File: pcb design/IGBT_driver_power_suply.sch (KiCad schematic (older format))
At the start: 41 parts, among them Q15 CSD19533Q5A, Q16 CSD19533Q5A, T1 TRANS-3-1CT, U2 LM5030

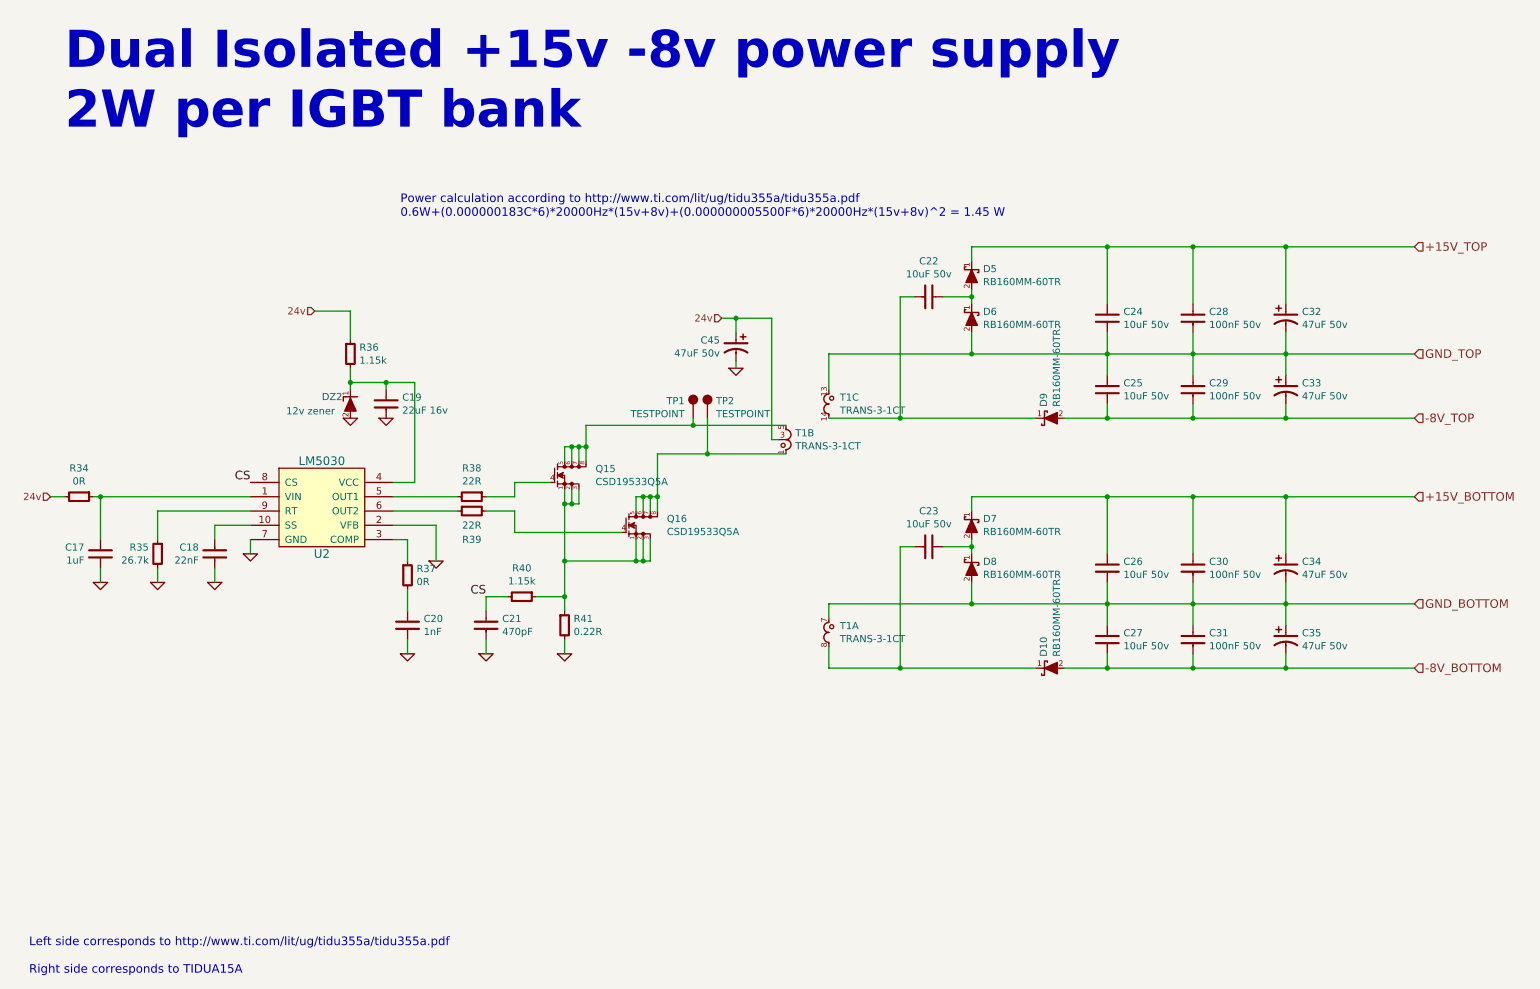
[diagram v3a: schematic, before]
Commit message: Added testpoints
Signed-off-by: Marcos Chaparro <mchaparro@paltatech.com>
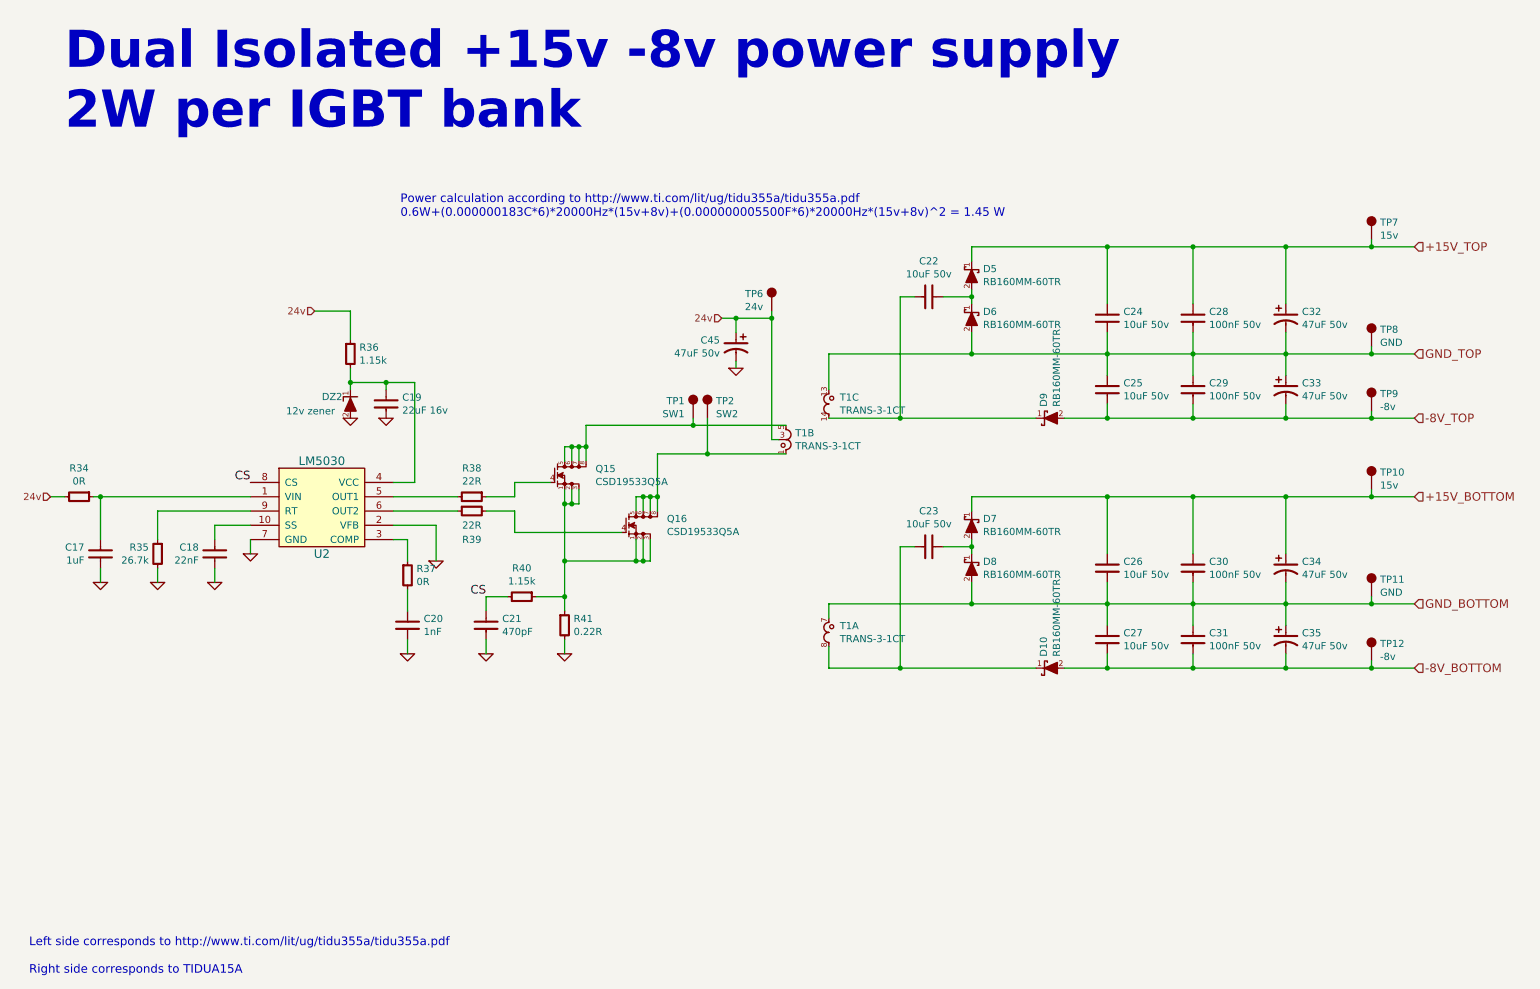
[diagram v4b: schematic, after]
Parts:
- added TP10, TP7: 15v, conn-test:TEST-SMD-SMALL, symbol TESTPOINT
- added TP11, TP8: GND, conn-test:TEST-SMD-SMALL, symbol TESTPOINT
- added TP12, TP9: -8v, conn-test:TEST-SMD-SMALL, symbol TESTPOINT
- added TP6: 24v, conn-test:TEST-SMD-SMALL, symbol TESTPOINT
- TP1: value TESTPOINT -> SW1
- TP2: value TESTPOINT -> SW2
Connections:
- net +15V_BOTTOM: now also TP10.1
- net +15V_TOP: now also TP7.1
- net -8V_BOTTOM: now also TP12.1
- net -8V_TOP: now also TP9.1
- net 24v: now also TP6.1
- net GND_BOTTOM: now also TP11.1
- net GND_TOP: now also TP8.1
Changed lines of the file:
@@
 $EndComp
 $Comp
-L GND #PWR06
+L GND #PWR11
 U 1 1 582356E3
 P 2950 3500
-F 0 "#PWR06" H 2950 3500 30  0001 C CNN
+F 0 "#PWR11" H 2950 3500 30  0001 C CNN
 F 1 "GND" H 2950 3430 30  0001 C CNN
 F 2 "" H 2950 3500 60  0000 C CNN
@@
 $EndComp
 $Comp
-L GND #PWR07
+L GND #PWR12
 U 1 1 58235BA0
 P 3200 3500
-F 0 "#PWR07" H 3200 3500 30  0001 C CNN
+F 0 "#PWR12" H 3200 3500 30  0001 C CNN
 F 1 "GND" H 3200 3430 30  0001 C CNN
 F 2 "" H 3200 3500 60  0000 C CNN
@@
 $EndComp
 $Comp
-L GND #PWR08
+L GND #PWR9
 U 1 1 58235E8A
 P 2000 4650
-F 0 "#PWR08" H 2000 4650 30  0001 C CNN
+F 0 "#PWR9" H 2000 4650 30  0001 C CNN
 F 1 "GND" H 2000 4580 30  0001 C CNN
 F 2 "" H 2000 4650 60  0000 C CNN
@@
 $EndComp
 $Comp
-L GND #PWR09
+L GND #PWR10
 U 1 1 58235EBE
 P 2250 4450
-F 0 "#PWR09" H 2250 4450 30  0001 C CNN
+F 0 "#PWR10" H 2250 4450 30  0001 C CNN
 F 1 "GND" H 2250 4380 30  0001 C CNN
 F 2 "" H 2250 4450 60  0000 C CNN
@@
 $EndComp
 $Comp
-L GND #PWR010
+L GND #PWR8
 U 1 1 582361AD
 P 1600 4650
-F 0 "#PWR010" H 1600 4650 30  0001 C CNN
+F 0 "#PWR8" H 1600 4650 30  0001 C CNN
 F 1 "GND" H 1600 4580 30  0001 C CNN
 F 2 "" H 1600 4650 60  0000 C CNN
@@
 $EndComp
 $Comp
-L GND #PWR011
+L GND #PWR15
 U 1 1 58236F6A
 P 3900 5150
-F 0 "#PWR011" H 3900 5150 30  0001 C CNN
+F 0 "#PWR15" H 3900 5150 30  0001 C CNN
 F 1 "GND" H 3900 5080 30  0001 C CNN
 F 2 "" H 3900 5150 60  0000 C CNN
@@
 $EndComp
 $Comp
-L GND #PWR012
+L GND #PWR16
 U 1 1 582370C3
 P 4450 5150
-F 0 "#PWR012" H 4450 5150 30  0001 C CNN
+F 0 "#PWR16" H 4450 5150 30  0001 C CNN
 F 1 "GND" H 4450 5080 30  0001 C CNN
 F 2 "" H 4450 5150 60  0000 C CNN
@@
 $EndComp
 $Comp
-L GND #PWR013
+L GND #PWR7
 U 1 1 582389B6
 P 1200 4650
-F 0 "#PWR013" H 1200 4650 30  0001 C CNN
+F 0 "#PWR7" H 1200 4650 30  0001 C CNN
 F 1 "GND" H 1200 4580 30  0001 C CNN
 F 2 "" H 1200 4650 60  0000 C CNN
@@
 $EndComp
 $Comp
-L GND #PWR014
+L GND #PWR14
 U 1 1 5823969B
 P 3550 4500
-F 0 "#PWR014" H 3550 4500 30  0001 C CNN
+F 0 "#PWR14" H 3550 4500 30  0001 C CNN
 F 1 "GND" H 3550 4430 30  0001 C CNN
 F 2 "" H 3550 4500 60  0000 C CNN
@@
 $EndComp
 $Comp
-L GND #PWR015
+L GND #PWR13
 U 1 1 582397EE
 P 3350 5150
-F 0 "#PWR015" H 3350 5150 30  0001 C CNN
+F 0 "#PWR13" H 3350 5150 30  0001 C CNN
 F 1 "GND" H 3350 5080 30  0001 C CNN
 F 2 "" H 3350 5150 60  0000 C CNN
@@
 P 5350 3500
 F 0 "TP1" H 5410 3621 50  0000 L CNN
-F 1 "TESTPOINT" H 5410 3530 50  0000 L CNN
+F 1 "SW1" H 5410 3530 50  0000 L CNN
 F 2 "conn-test:TEST-SMD-SMALL" H 5350 3500 50  0001 C CNN
 F 3 "" H 5350 3500 50  0000 C CNN
@@
 	4450 5150 4450 5050
 Wire Wire Line
-	2950 2950 2950 2750
+	2950 2750 2950 2950
 Wire Wire Line
 	2950 2750 2700 2750
@@
 P 5450 3500
 F 0 "TP2" H 5510 3621 50  0000 L CNN
-F 1 "TESTPOINT" H 5510 3530 50  0000 L CNN
+F 1 "SW2" H 5510 3530 50  0000 L CNN
 F 2 "conn-test:TEST-SMD-SMALL" H 5450 3500 50  0001 C CNN
 F 3 "" H 5450 3500 50  0000 C CNN
@@
 	5900 3650 5950 3650
 Wire Wire Line
-	5900 2800 5900 3650
+	5900 2750 5900 3650
 $Comp
 L C-ALUM-6.3mm C45
@@
 Connection ~ 5650 2800
 $Comp
-L GND #PWR016
+L GND #PWR17
 U 1 1 5827420A
 P 5650 3150
-F 0 "#PWR016" H 5650 3150 30  0001 C CNN
+F 0 "#PWR17" H 5650 3150 30  0001 C CNN
 F 1 "GND" H 5650 3080 30  0001 C CNN
 F 2 "" H 5650 3150 60  0000 C CNN
@@
 Text HLabel 850  4050 0    50   Input ~ 0
 24v
+$Comp
+L TESTPOINT TP8
+U 1 1 583622CC
+P 10100 3000
+F 0 "TP8" H 10160 3121 50  0000 L CNN
+F 1 "GND" H 10160 3030 50  0000 L CNN
+F 2 "conn-test:TEST-SMD-SMALL" H 10100 3000 50  0001 C CNN
+F 3 "" H 10100 3000 50  0000 C CNN
+	1    10100 3000
+	1    0    0    -1
+$EndComp
+$Comp
+L TESTPOINT TP7
+U 1 1 583622D2
+P 10100 2250
+F 0 "TP7" H 10160 2371 50  0000 L CNN
+F 1 "15v" H 10160 2280 50  0000 L CNN
+F 2 "conn-test:TEST-SMD-SMALL" H 10100 2250 50  0001 C CNN
+F 3 "" H 10100 2250 50  0000 C CNN
+	1    10100 2250
+	1    0    0    -1
+$EndComp
+Wire Wire Line
+	10100 3000 10100 3050
+Connection ~ 10100 3050
+$Comp
+L TESTPOINT TP9
+U 1 1 58362CA0
+P 10100 3450
+F 0 "TP9" H 10160 3571 50  0000 L CNN
+F 1 "-8v" H 10160 3480 50  0000 L CNN
+F 2 "conn-test:TEST-SMD-SMALL" H 10100 3450 50  0001 C CNN
+F 3 "" H 10100 3450 50  0000 C CNN
+	1    10100 3450
+	1    0    0    -1
+$EndComp
+Wire Wire Line
+	10100 3450 10100 3500
+Connection ~ 10100 3500
+Wire Wire Line
+	10100 2250 10100 2300
+Connection ~ 10100 2300
+$Comp
+L TESTPOINT TP10
+U 1 1 583635A2
+P 10100 4000
+F 0 "TP10" H 10160 4121 50  0000 L CNN
+F 1 "15v" H 10160 4030 50  0000 L CNN
+F 2 "conn-test:TEST-SMD-SMALL" H 10100 4000 50  0001 C CNN
+F 3 "" H 10100 4000 50  0000 C CNN
+	1    10100 4000
+	1    0    0    -1
+$EndComp
+$Comp
+L TESTPOINT TP11
+U 1 1 5836369A
+P 10100 4750
+F 0 "TP11" H 10160 4871 50  0000 L CNN
+F 1 "GND" H 10160 4780 50  0000 L CNN
+F 2 "conn-test:TEST-SMD-SMALL" H 10100 4750 50  0001 C CNN
+F 3 "" H 10100 4750 50  0000 C CNN
+	1    10100 4750
+	1    0    0    -1
+$EndComp
+$Comp
+L TESTPOINT TP12
+U 1 1 58363914
+P 10100 5200
+F 0 "TP12" H 10160 5321 50  0000 L CNN
+F 1 "-8v" H 10160 5230 50  0000 L CNN
+F 2 "conn-test:TEST-SMD-SMALL" H 10100 5200 50  0001 C CNN
+F 3 "" H 10100 5200 50  0000 C CNN
+	1    10100 5200
+	1    0    0    -1
+$EndComp
+Wire Wire Line
+	10100 5200 10100 5250
+Connection ~ 10100 5250
+Wire Wire Line
+	10100 4750 10100 4800
+Connection ~ 10100 4800
+Wire Wire Line
+	10100 4000 10100 4050
+Connection ~ 10100 4050
+$Comp
+L TESTPOINT TP6
+U 1 1 583605D7
+P 5900 2750
+F 0 "TP6" H 5960 2871 50  0000 L CNN
+F 1 "24v" H 5960 2780 50  0000 L CNN
+F 2 "conn-test:TEST-SMD-SMALL" H 5900 2750 50  0001 C CNN
+F 3 "" H 5900 2750 50  0000 C CNN
+	1    5900 2750
+	-1   0    0    -1
+$EndComp
+Connection ~ 5900 2800
 $EndSCHEMATC

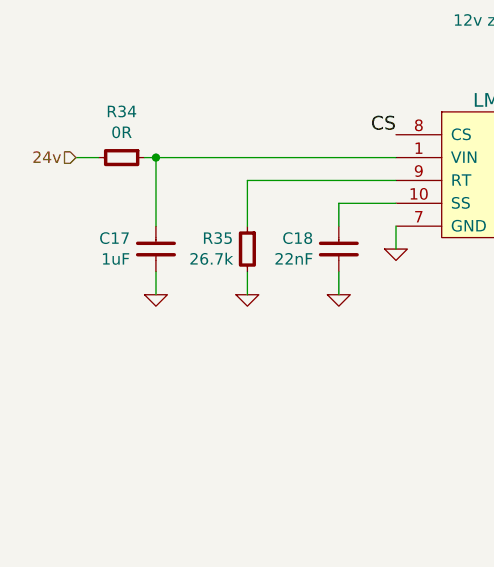
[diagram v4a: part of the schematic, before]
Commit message: Added NAND gates for shoot-through protection, and to configure the driver so when a fault is asserted the whole inverter will be shut down until a reset signal is issued
Signed-off-by: Marcos Chaparro <mchaparro@paltatech.com>
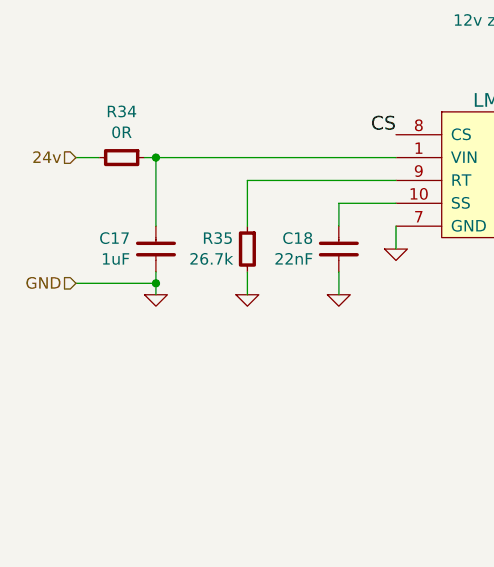
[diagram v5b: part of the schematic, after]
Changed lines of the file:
@@
 $EndComp
 $Comp
-L GND #PWR11
+L GND #PWR010
 U 1 1 582356E3
 P 2950 3500
-F 0 "#PWR11" H 2950 3500 30  0001 C CNN
+F 0 "#PWR010" H 2950 3500 30  0001 C CNN
 F 1 "GND" H 2950 3430 30  0001 C CNN
 F 2 "" H 2950 3500 60  0000 C CNN
@@
 $EndComp
 $Comp
-L GND #PWR12
+L GND #PWR011
 U 1 1 58235BA0
 P 3200 3500
-F 0 "#PWR12" H 3200 3500 30  0001 C CNN
+F 0 "#PWR011" H 3200 3500 30  0001 C CNN
 F 1 "GND" H 3200 3430 30  0001 C CNN
 F 2 "" H 3200 3500 60  0000 C CNN
@@
 $EndComp
 $Comp
-L GND #PWR9
+L GND #PWR012
 U 1 1 58235E8A
 P 2000 4650
-F 0 "#PWR9" H 2000 4650 30  0001 C CNN
+F 0 "#PWR012" H 2000 4650 30  0001 C CNN
 F 1 "GND" H 2000 4580 30  0001 C CNN
 F 2 "" H 2000 4650 60  0000 C CNN
@@
 $EndComp
 $Comp
-L GND #PWR10
+L GND #PWR013
 U 1 1 58235EBE
 P 2250 4450
-F 0 "#PWR10" H 2250 4450 30  0001 C CNN
+F 0 "#PWR013" H 2250 4450 30  0001 C CNN
 F 1 "GND" H 2250 4380 30  0001 C CNN
 F 2 "" H 2250 4450 60  0000 C CNN
@@
 $EndComp
 $Comp
-L GND #PWR8
+L GND #PWR014
 U 1 1 582361AD
 P 1600 4650
-F 0 "#PWR8" H 1600 4650 30  0001 C CNN
+F 0 "#PWR014" H 1600 4650 30  0001 C CNN
 F 1 "GND" H 1600 4580 30  0001 C CNN
 F 2 "" H 1600 4650 60  0000 C CNN
@@
 $EndComp
 $Comp
-L GND #PWR15
+L GND #PWR015
 U 1 1 58236F6A
 P 3900 5150
-F 0 "#PWR15" H 3900 5150 30  0001 C CNN
+F 0 "#PWR015" H 3900 5150 30  0001 C CNN
 F 1 "GND" H 3900 5080 30  0001 C CNN
 F 2 "" H 3900 5150 60  0000 C CNN
@@
 $EndComp
 $Comp
-L GND #PWR16
+L GND #PWR016
 U 1 1 582370C3
 P 4450 5150
-F 0 "#PWR16" H 4450 5150 30  0001 C CNN
+F 0 "#PWR016" H 4450 5150 30  0001 C CNN
 F 1 "GND" H 4450 5080 30  0001 C CNN
 F 2 "" H 4450 5150 60  0000 C CNN
@@
 $EndComp
 $Comp
-L GND #PWR7
+L GND #PWR017
 U 1 1 582389B6
 P 1200 4650
-F 0 "#PWR7" H 1200 4650 30  0001 C CNN
+F 0 "#PWR017" H 1200 4650 30  0001 C CNN
 F 1 "GND" H 1200 4580 30  0001 C CNN
 F 2 "" H 1200 4650 60  0000 C CNN
@@
 $EndComp
 $Comp
-L GND #PWR14
+L GND #PWR018
 U 1 1 5823969B
 P 3550 4500
-F 0 "#PWR14" H 3550 4500 30  0001 C CNN
+F 0 "#PWR018" H 3550 4500 30  0001 C CNN
 F 1 "GND" H 3550 4430 30  0001 C CNN
 F 2 "" H 3550 4500 60  0000 C CNN
@@
 $EndComp
 $Comp
-L GND #PWR13
+L GND #PWR019
 U 1 1 582397EE
 P 3350 5150
-F 0 "#PWR13" H 3350 5150 30  0001 C CNN
+F 0 "#PWR019" H 3350 5150 30  0001 C CNN
 F 1 "GND" H 3350 5080 30  0001 C CNN
 F 2 "" H 3350 5150 60  0000 C CNN
@@
 Connection ~ 5650 2800
 $Comp
-L GND #PWR17
+L GND #PWR020
 U 1 1 5827420A
 P 5650 3150
-F 0 "#PWR17" H 5650 3150 30  0001 C CNN
+F 0 "#PWR020" H 5650 3150 30  0001 C CNN
 F 1 "GND" H 5650 3080 30  0001 C CNN
 F 2 "" H 5650 3150 60  0000 C CNN
@@
 $EndComp
 Connection ~ 5900 2800
+Text HLabel 850  4600 0    50   Input ~ 0
+GND
+Wire Wire Line
+	850  4600 1200 4600
+Connection ~ 1200 4600
 $EndSCHEMATC

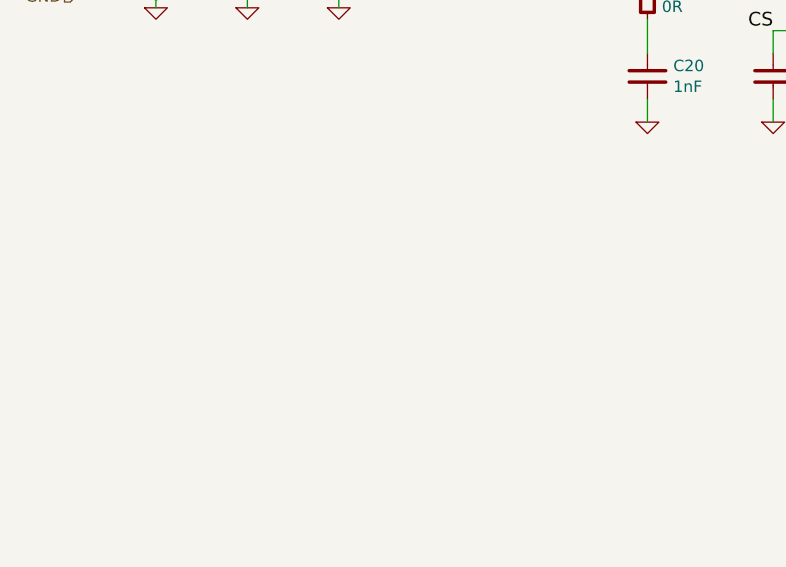
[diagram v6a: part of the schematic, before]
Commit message: Added gate voltage control, more decoupling pads for the buffer transistors, added notes
Signed-off-by: Marcos Chaparro <mchaparro@paltatech.com>
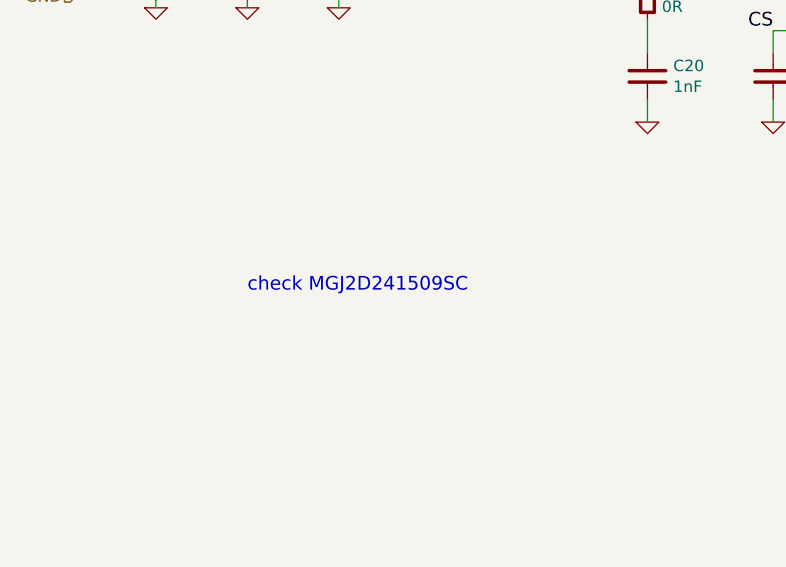
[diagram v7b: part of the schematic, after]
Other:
- note added: "check MGJ2D241509SC"
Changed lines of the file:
@@
 $Descr A4 11693 8268
 encoding utf-8
-Sheet 3 4
+Sheet 4 6
 Title ""
 Date "2016-11-09"
@@
 $EndComp
 $Comp
-L GND #PWR012
+L GND #PWR18
 U 1 1 582356E3
 P 2950 3500
-F 0 "#PWR012" H 2950 3500 30  0001 C CNN
+F 0 "#PWR18" H 2950 3500 30  0001 C CNN
 F 1 "GND" H 2950 3430 30  0001 C CNN
 F 2 "" H 2950 3500 60  0000 C CNN
@@
 $EndComp
 $Comp
-L GND #PWR013
+L GND #PWR19
 U 1 1 58235BA0
 P 3200 3500
-F 0 "#PWR013" H 3200 3500 30  0001 C CNN
+F 0 "#PWR19" H 3200 3500 30  0001 C CNN
 F 1 "GND" H 3200 3430 30  0001 C CNN
 F 2 "" H 3200 3500 60  0000 C CNN
@@
 $EndComp
 $Comp
-L GND #PWR014
+L GND #PWR16
 U 1 1 58235E8A
 P 2000 4650
-F 0 "#PWR014" H 2000 4650 30  0001 C CNN
+F 0 "#PWR16" H 2000 4650 30  0001 C CNN
 F 1 "GND" H 2000 4580 30  0001 C CNN
 F 2 "" H 2000 4650 60  0000 C CNN
@@
 $EndComp
 $Comp
-L GND #PWR015
+L GND #PWR17
 U 1 1 58235EBE
 P 2250 4450
-F 0 "#PWR015" H 2250 4450 30  0001 C CNN
+F 0 "#PWR17" H 2250 4450 30  0001 C CNN
 F 1 "GND" H 2250 4380 30  0001 C CNN
 F 2 "" H 2250 4450 60  0000 C CNN
@@
 $EndComp
 $Comp
-L GND #PWR016
+L GND #PWR15
 U 1 1 582361AD
 P 1600 4650
-F 0 "#PWR016" H 1600 4650 30  0001 C CNN
+F 0 "#PWR15" H 1600 4650 30  0001 C CNN
 F 1 "GND" H 1600 4580 30  0001 C CNN
 F 2 "" H 1600 4650 60  0000 C CNN
@@
 $EndComp
 $Comp
-L GND #PWR017
+L GND #PWR22
 U 1 1 58236F6A
 P 3900 5150
-F 0 "#PWR017" H 3900 5150 30  0001 C CNN
+F 0 "#PWR22" H 3900 5150 30  0001 C CNN
 F 1 "GND" H 3900 5080 30  0001 C CNN
 F 2 "" H 3900 5150 60  0000 C CNN
@@
 $EndComp
 $Comp
-L GND #PWR018
+L GND #PWR23
 U 1 1 582370C3
 P 4450 5150
-F 0 "#PWR018" H 4450 5150 30  0001 C CNN
+F 0 "#PWR23" H 4450 5150 30  0001 C CNN
 F 1 "GND" H 4450 5080 30  0001 C CNN
 F 2 "" H 4450 5150 60  0000 C CNN
@@
 $EndComp
 $Comp
-L GND #PWR019
+L GND #PWR14
 U 1 1 582389B6
 P 1200 4650
-F 0 "#PWR019" H 1200 4650 30  0001 C CNN
+F 0 "#PWR14" H 1200 4650 30  0001 C CNN
 F 1 "GND" H 1200 4580 30  0001 C CNN
 F 2 "" H 1200 4650 60  0000 C CNN
@@
 $EndComp
 $Comp
-L GND #PWR020
+L GND #PWR21
 U 1 1 5823969B
 P 3550 4500
-F 0 "#PWR020" H 3550 4500 30  0001 C CNN
+F 0 "#PWR21" H 3550 4500 30  0001 C CNN
 F 1 "GND" H 3550 4430 30  0001 C CNN
 F 2 "" H 3550 4500 60  0000 C CNN
@@
 $EndComp
 $Comp
-L GND #PWR021
+L GND #PWR20
 U 1 1 582397EE
 P 3350 5150
-F 0 "#PWR021" H 3350 5150 30  0001 C CNN
+F 0 "#PWR20" H 3350 5150 30  0001 C CNN
 F 1 "GND" H 3350 5080 30  0001 C CNN
 F 2 "" H 3350 5150 60  0000 C CNN
@@
 Connection ~ 5650 2800
 $Comp
-L GND #PWR022
+L GND #PWR24
 U 1 1 5827420A
 P 5650 3150
-F 0 "#PWR022" H 5650 3150 30  0001 C CNN
+F 0 "#PWR24" H 5650 3150 30  0001 C CNN
 F 1 "GND" H 5650 3080 30  0001 C CNN
 F 2 "" H 5650 3150 60  0000 C CNN
@@
 	850  4600 1200 4600
 Connection ~ 1200 4600
+Text Notes 1600 5900 0    60   ~ 0
+check MGJ2D241509SC
 $EndSCHEMATC
